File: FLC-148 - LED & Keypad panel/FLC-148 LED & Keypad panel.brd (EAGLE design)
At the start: 52 x 73.8 mm, 76 parts, among them IC1 MAX6818, IC2 MAX6818, IC3 NTGD3148NT1G, IC4 NTGD3148NT1G, IC5 STM32G071CBU6, IC6 ECS-480-10-33B-CKM-TR, J1 FTSH-107-01-L-DV-K-A

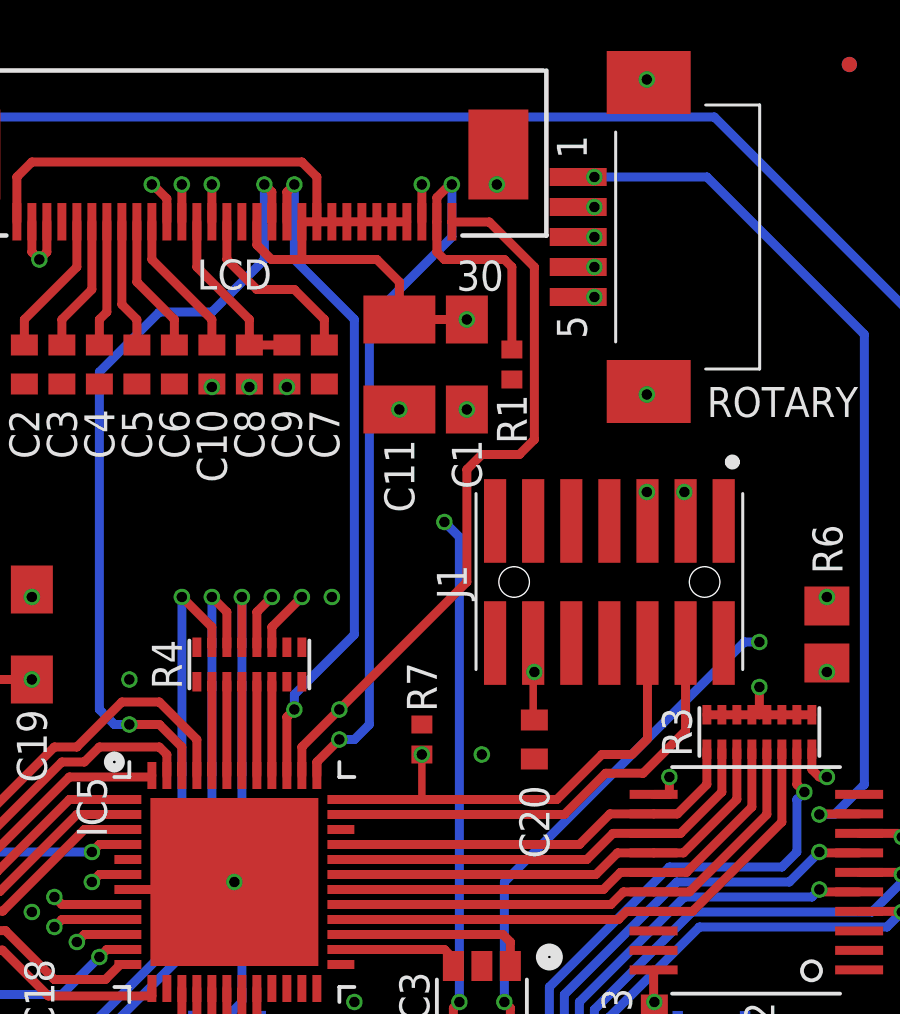
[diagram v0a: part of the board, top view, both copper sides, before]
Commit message: - routed missing LCD D/C pin to PA12
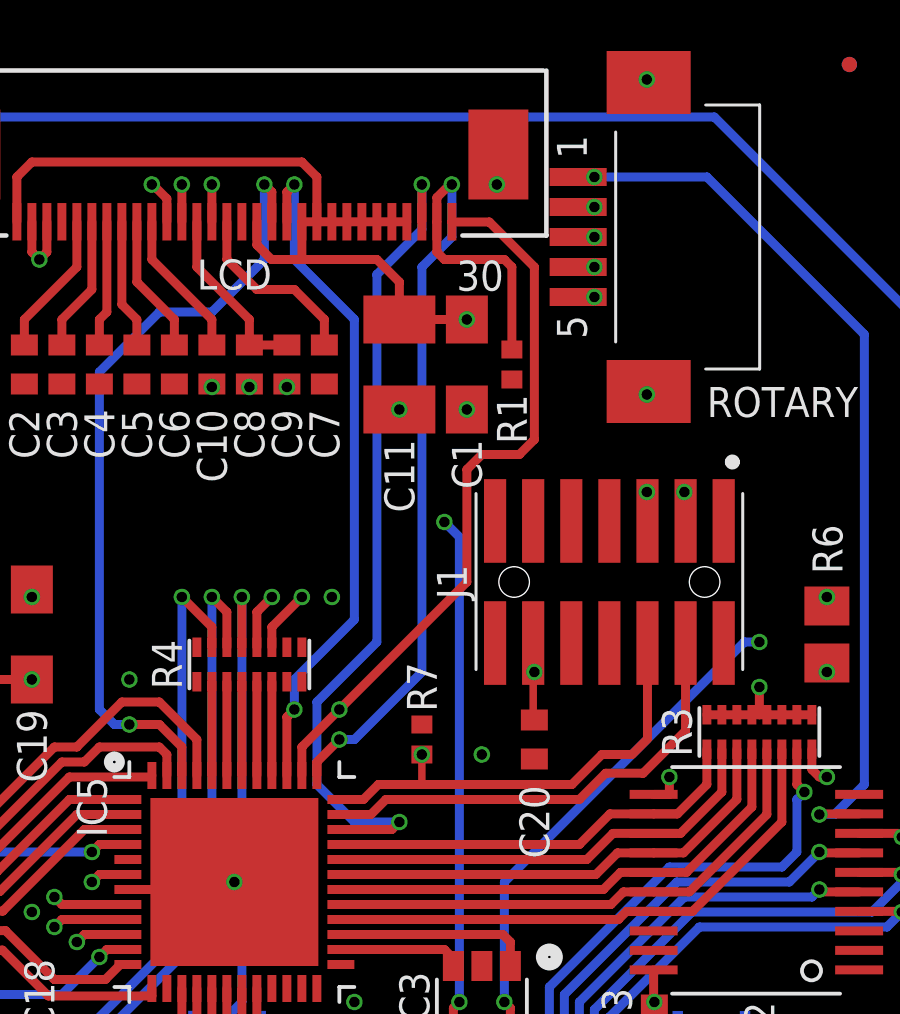
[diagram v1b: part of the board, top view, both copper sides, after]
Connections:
- net OLED_!D!/C: now also IC5.34_PA12[PA10]
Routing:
- net OLED_!D!/C: track 1.24 -> 28.0 mm, vias 1 -> 2
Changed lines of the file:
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@@
 <grid distance="0.25" unitdist="mm" unit="mm" style="dots" multiple="1" display="yes" altdistance="0.05" altunitdist="mm" altunit="mm"/>
 <layers>
-<layer number="1" name="Top" color="4" fill="1" visible="no" active="yes"/>
+<layer number="1" name="Top" color="4" fill="1" visible="yes" active="yes"/>
 <layer number="2" name="Route2" color="16" fill="1" visible="no" active="yes"/>
 <layer number="3" name="Route3" color="17" fill="1" visible="no" active="no"/>
@@
 <layer number="14" name="Route14" color="22" fill="1" visible="no" active="no"/>
 <layer number="15" name="Route15" color="23" fill="1" visible="no" active="yes"/>
-<layer number="16" name="Bottom" color="1" fill="1" visible="yes" active="yes"/>
+<layer number="16" name="Bottom" color="1" fill="1" visible="no" active="yes"/>
 <layer number="17" name="Pads" color="2" fill="1" visible="yes" active="yes"/>
 <layer number="18" name="Vias" color="2" fill="1" visible="yes" active="yes"/>
 <layer number="19" name="Unrouted" color="6" fill="1" visible="yes" active="yes"/>
 <layer number="20" name="Dimension" color="24" fill="1" visible="yes" active="yes"/>
-<layer number="21" name="tPlace" color="7" fill="1" visible="no" active="yes"/>
-<layer number="22" name="bPlace" color="7" fill="1" visible="yes" active="yes"/>
-<layer number="23" name="tOrigins" color="15" fill="1" visible="no" active="yes"/>
-<layer number="24" name="bOrigins" color="15" fill="1" visible="yes" active="yes"/>
-<layer number="25" name="tNames" color="7" fill="1" visible="no" active="yes"/>
-<layer number="26" name="bNames" color="7" fill="1" visible="yes" active="yes"/>
+<layer number="21" name="tPlace" color="7" fill="1" visible="yes" active="yes"/>
+<layer number="22" name="bPlace" color="7" fill="1" visible="no" active="yes"/>
+<layer number="23" name="tOrigins" color="15" fill="1" visible="yes" active="yes"/>
+<layer number="24" name="bOrigins" color="15" fill="1" visible="no" active="yes"/>
+<layer number="25" name="tNames" color="7" fill="1" visible="yes" active="yes"/>
+<layer number="26" name="bNames" color="7" fill="1" visible="no" active="yes"/>
 <layer number="27" name="tValues" color="7" fill="1" visible="no" active="yes"/>
 <layer number="28" name="bValues" color="7" fill="1" visible="no" active="yes"/>
-<layer number="29" name="tStop" color="7" fill="3" visible="no" active="yes"/>
-<layer number="30" name="bStop" color="7" fill="6" visible="yes" active="yes"/>
+<layer number="29" name="tStop" color="7" fill="3" visible="yes" active="yes"/>
+<layer number="30" name="bStop" color="7" fill="6" visible="no" active="yes"/>
 <layer number="31" name="tCream" color="7" fill="4" visible="no" active="yes"/>
 <layer number="32" name="bCream" color="7" fill="5" visible="no" active="yes"/>
@@
 <layer number="37" name="tTest" color="7" fill="1" visible="no" active="yes"/>
 <layer number="38" name="bTest" color="7" fill="1" visible="no" active="yes"/>
-<layer number="39" name="tKeepout" color="4" fill="11" visible="no" active="yes"/>
-<layer number="40" name="bKeepout" color="1" fill="11" visible="yes" active="yes"/>
-<layer number="41" name="tRestrict" color="4" fill="10" visible="no" active="yes"/>
-<layer number="42" name="bRestrict" color="1" fill="10" visible="yes" active="yes"/>
+<layer number="39" name="tKeepout" color="4" fill="11" visible="yes" active="yes"/>
+<layer number="40" name="bKeepout" color="1" fill="11" visible="no" active="yes"/>
+<layer number="41" name="tRestrict" color="4" fill="10" visible="yes" active="yes"/>
+<layer number="42" name="bRestrict" color="1" fill="10" visible="no" active="yes"/>
 <layer number="43" name="vRestrict" color="2" fill="10" visible="yes" active="yes"/>
 <layer number="44" name="Drills" color="7" fill="1" visible="no" active="yes"/>
@@
 <layer number="49" name="Reference" color="7" fill="1" visible="no" active="yes"/>
 <layer number="50" name="dxf" color="7" fill="1" visible="no" active="no"/>
-<layer number="51" name="tDocu" color="7" fill="1" visible="no" active="yes"/>
-<layer number="52" name="bDocu" color="7" fill="1" visible="yes" active="yes"/>
+<layer number="51" name="tDocu" color="7" fill="1" visible="yes" active="yes"/>
+<layer number="52" name="bDocu" color="7" fill="1" visible="no" active="yes"/>
 <layer number="53" name="tGND_GNDA" color="7" fill="1" visible="no" active="no"/>
 <layer number="54" name="bGND_GNDA" color="7" fill="1" visible="no" active="no"/>
@@
 <contactref element="J1" pad="4"/>
 <contactref element="IC5" pad="35_PA13"/>
-<wire x1="29.8" y1="35" x2="37.25" y2="35" width="0.3" layer="1"/>
-<wire x1="37.25" y1="35" x2="38.625" y2="36.375" width="0.3" layer="1"/>
+<wire x1="37.75" y1="35.5" x2="31.3" y2="35.5" width="0.3" layer="1"/>
+<wire x1="31.3" y1="35.5" x2="30.8" y2="35" width="0.3" layer="1"/>
+<wire x1="29.8" y1="35" x2="30.8" y2="35" width="0.3" layer="1"/>
+<wire x1="37.75" y1="35.5" x2="38.625" y2="36.375" width="0.3" layer="1"/>
 <wire x1="38.625" y1="36.375" x2="39.875" y2="36.375" width="0.3" layer="1"/>
 <wire x1="39.875" y1="36.375" x2="41.29" y2="37.79" width="0.3" layer="1"/>
@@
 <wire x1="29" y1="36.3" x2="29" y2="36.75" width="0.3" layer="1"/>
 <wire x1="29.75" y1="37.5" x2="29" y2="36.75" width="0.3" layer="1"/>
-<wire x1="30.25" y1="37.5" x2="30.75" y2="38" width="0.3" layer="16"/>
+<wire x1="30.25" y1="37.5" x2="32.5" y2="39.75" width="0.3" layer="16"/>
 <wire x1="29.75" y1="37.5" x2="30.25" y2="37.5" width="0.3" layer="16"/>
-<wire x1="30.75" y1="38" x2="30.75" y2="51.5" width="0.3" layer="16"/>
-<wire x1="30.75" y1="51.5" x2="33.5" y2="54.25" width="0.3" layer="16"/>
+<wire x1="32.5" y1="39.75" x2="32.5" y2="53.25" width="0.3" layer="16"/>
+<wire x1="32.5" y1="53.25" x2="33.5" y2="54.25" width="0.3" layer="16"/>
 <wire x1="35.5" y1="50.5" x2="35.5" y2="53.25" width="0.3" layer="1"/>
 <wire x1="35.25" y1="53.5" x2="33.25" y2="53.5" width="0.3" layer="1"/>
@@
 <via x="32.5" y="56" extent="1-16" drill="0.35"/>
 <wire x1="32.5" y1="54.757" x2="32.5" y2="56" width="0.3" layer="1"/>
+<contactref element="IC5" pad="34_PA12[PA10]"/>
+<via x="31.75" y="34.75" extent="1-16" drill="0.35"/>
+<wire x1="29.8" y1="34.5" x2="31.5" y2="34.5" width="0.3" layer="1"/>
+<wire x1="31.5" y1="34.5" x2="31.75" y2="34.75" width="0.3" layer="1"/>
+<wire x1="31.75" y1="34.75" x2="30.25" y2="34.75" width="0.3" layer="16"/>
+<wire x1="30.25" y1="34.75" x2="29" y2="36" width="0.3" layer="16"/>
+<wire x1="29" y1="38.75" x2="31" y2="40.75" width="0.3" layer="16"/>
+<wire x1="29" y1="36" x2="29" y2="38.75" width="0.3" layer="16"/>
+<wire x1="32.5" y1="54.5" x2="32.5" y2="56" width="0.3" layer="16"/>
+<wire x1="31" y1="40.75" x2="31" y2="53" width="0.3" layer="16"/>
+<wire x1="31" y1="53" x2="32.5" y2="54.5" width="0.3" layer="16"/>
 </signal>
 <signal name="MCU_KEYPAD_INTERRUPT" class="2">
@@
 <contactref element="J1" pad="6"/>
 <contactref element="IC5" pad="36_PA14-BOOT0"/>
-<wire x1="37" y1="35.5" x2="32.5" y2="35.5" width="0.3" layer="1"/>
-<wire x1="32.5" y1="35.5" x2="29.8" y2="35.5" width="0.3" layer="1"/>
-<wire x1="37" y1="35.5" x2="38.5" y2="37" width="0.3" layer="1"/>
+<wire x1="37.5" y1="36" x2="32.25" y2="36" width="0.3" layer="1"/>
+<wire x1="32.5" y1="36" x2="31.05" y2="36" width="0.3" layer="1"/>
+<wire x1="31.05" y1="36" x2="30.55" y2="35.5" width="0.3" layer="1"/>
+<wire x1="30.55" y1="35.5" x2="29.8" y2="35.5" width="0.3" layer="1"/>
+<wire x1="37.5" y1="36" x2="38.5" y2="37" width="0.3" layer="1"/>
 <wire x1="38.5" y1="37" x2="39.5" y2="37" width="0.3" layer="1"/>
 <wire x1="39.5" y1="37" x2="40.02" y2="37.52" width="0.3" layer="1"/>
 <wire x1="40.02" y1="37.52" x2="40.02" y2="40.715" width="0.3" layer="1"/>
 <contactref element="R7" pad="2"/>
-<wire x1="32.5" y1="37" x2="32.5" y2="35.5" width="0.25" layer="1"/>
+<wire x1="32.5" y1="37" x2="32.5" y2="36" width="0.25" layer="1"/>
 <contactref element="MCU" pad="12_PD14"/>
 <via x="24.5" y="20.75" extent="1-16" drill="0.35"/>
@@
 <wire x1="28.25" y1="38.5" x2="28" y2="38.25" width="0.3" layer="1"/>
 <wire x1="28" y1="36.3" x2="28" y2="38.25" width="0.3" layer="1"/>
-<wire x1="28.25" y1="38.5" x2="28.25" y2="39" width="0.3" layer="16"/>
-<wire x1="30.25" y1="41" x2="28.25" y2="39" width="0.3" layer="16"/>
-<wire x1="30.25" y1="41" x2="30.25" y2="51.5" width="0.3" layer="16"/>
+<wire x1="28.25" y1="38.5" x2="28.25" y2="39.5" width="0.3" layer="16"/>
+<wire x1="30.25" y1="41.5" x2="28.25" y2="39.5" width="0.3" layer="16"/>
+<wire x1="30.25" y1="41.5" x2="30.25" y2="51.5" width="0.3" layer="16"/>
 <wire x1="30.25" y1="51.5" x2="28.25" y2="53.5" width="0.3" layer="16"/>
 <wire x1="28.25" y1="53.5" x2="28.25" y2="56" width="0.3" layer="16"/>
@@
 <wire x1="40.225" y1="35.67" x2="40.75" y2="35.67" width="0.3" layer="1"/>
 <wire x1="40.75" y1="35.67" x2="40.75" y2="36.25" width="0.3" layer="1"/>
-<wire x1="30.5" y1="35.25" x2="25.5" y2="30.25" width="0.4" layer="2"/>
+<wire x1="30.75" y1="35.5" x2="25.5" y2="30.25" width="0.4" layer="2"/>
 <wire x1="21.75" y1="30.25" x2="25.5" y2="30.25" width="0.4" layer="2"/>
-<wire x1="39.75" y1="35.25" x2="40.75" y2="36.25" width="0.4" layer="2"/>
-<wire x1="39.75" y1="35.25" x2="30.5" y2="35.25" width="0.4" layer="2"/>
+<wire x1="40" y1="35.5" x2="40.75" y2="36.25" width="0.4" layer="2"/>
+<wire x1="40" y1="35.5" x2="30.75" y2="35.5" width="0.4" layer="2"/>
 </signal>
 <signal name="VBAT">

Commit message: - renamed signals to be more consistent
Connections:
- net BACKLIGHT_GREEN_DRAIN renamed LCD_BACKLIGHT_GREEN_DRAIN
- net BACKLIGHT_IR_DRAIN renamed LCD_BACKLIGHT_IR_DRAIN
- net KEYPAD_IR_LED_DRAIN renamed KEYPAD_BACKLIGHT_IR_DRAIN
- net LED_BACKLIGHT_GREEN_GATE renamed OLED_BACKLIGHT_GREEN_GATE
- net LED_BACKLIGHT_IR_GATE renamed OLED_BACKLIGHT_IR_GATE
- net SPI_LCD_MOSI renamed SPI_OLED_MOSI
- net SPI_LCD_SCK renamed SPI_OLED_SCK
- net SPI_LCD_SS renamed SPI_OLED_SS
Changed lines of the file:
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@@
 <wire x1="26.75" y1="22.4925125" x2="26.75" y2="18.96" width="0.3" layer="1"/>
 </signal>
-<signal name="SPI_LCD_SCK" class="2">
+<signal name="SPI_OLED_SCK" class="2">
 <contactref element="LCD" pad="19_DB6"/>
 <via x="28.25" y="56" extent="1-16" drill="0.35"/>
@@
 <wire x1="28.25" y1="53.5" x2="28.25" y2="56" width="0.3" layer="16"/>
 </signal>
-<signal name="SPI_LCD_MOSI" class="2">
+<signal name="SPI_OLED_MOSI" class="2">
 <contactref element="LCD" pad="18_DB7"/>
 <via x="27.25" y="56" extent="1-16" drill="0.35"/>
@@
 <wire x1="21.75" y1="49.75" x2="21.75" y2="38.5" width="0.3" layer="16"/>
 </signal>
-<signal name="SPI_LCD_SS" class="2">
+<signal name="SPI_OLED_SS" class="2">
 <contactref element="LCD" pad="30_!CS1!"/>
 <contactref element="IC5" pad="38_PD0"/>
@@
 <wire x1="34" y1="42.75" x2="34" y2="46.5" width="0.3" layer="1"/>
 </signal>
-<signal name="LED_BACKLIGHT_GREEN_GATE" class="2">
+<signal name="OLED_BACKLIGHT_GREEN_GATE" class="2">
 <contactref element="IC5" pad="27_PB15"/>
 <contactref element="IC3" pad="1_G1"/>
@@
 <wire x1="29.8" y1="31" x2="35.2" y2="31" width="0.3" layer="1"/>
 </signal>
-<signal name="LED_BACKLIGHT_IR_GATE" class="2">
+<signal name="OLED_BACKLIGHT_IR_GATE" class="2">
 <contactref element="IC5" pad="26_PB14"/>
 <contactref element="IC3" pad="3_G2"/>
@@
 <wire x1="46" y1="41.95" x2="46" y2="42.25" width="0.3" layer="1"/>
 </signal>
-<signal name="BACKLIGHT_GREEN_DRAIN" class="2">
+<signal name="LCD_BACKLIGHT_GREEN_DRAIN" class="2">
 <contactref element="IC3" pad="6_D1"/>
 <via x="35.25" y="28.75" extent="1-16" drill="0.35"/>
@@
 <wire x1="50.45" y1="40.75" x2="50.5" y2="40.8" width="0.3" layer="16"/>
 </signal>
-<signal name="BACKLIGHT_IR_DRAIN" class="2">
+<signal name="LCD_BACKLIGHT_IR_DRAIN" class="2">
 <contactref element="IC3" pad="4_D2"/>
 <via x="33.75" y="28.75" extent="1-16" drill="0.35"/>
@@
 <wire x1="48.25" y1="44.25" x2="48.25" y2="44.75" width="0.4" layer="2"/>
 </signal>
-<signal name="KEYPAD_IR_LED_DRAIN" class="2">
+<signal name="KEYPAD_BACKLIGHT_IR_DRAIN" class="2">
 <contactref element="LED5" pad="C"/>
 <contactref element="LED8" pad="C"/>

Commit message: - replaced 1mm 5p zif connector (52793-0570) with better part (52207-0533)
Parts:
- PTT, ROTARY: value 52793-0570 -> 52207-0533
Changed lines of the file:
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@@
 <attribute name="VALUE" x="43.75" y="35.75" size="1" layer="27" font="vector" align="center"/>
 </element>
-<element name="PTT" library="527930570 FFC Connector 5p 1mm Pitch" package="SMD" value="52793-0570" x="37.75" y="15" smashed="yes" rot="R90">
+<element name="PTT" library="527930570 FFC Connector 5p 1mm Pitch" package="SMD" value="52207-0533" x="37.75" y="15" smashed="yes" rot="R90">
 <attribute name="NAME" x="38.25" y="9.5" size="1" layer="25" font="vector" rot="R180" align="center-right"/>
 <attribute name="VALUE" x="41.75" y="15" size="1" layer="27" font="vector" rot="R90" align="center"/>
@@
 <attribute name="VALUE" x="19.155" y="40.365" size="1.27" layer="27" rot="R90"/>
 </element>
-<element name="ROTARY" library="527930570 FFC Connector 5p 1mm Pitch" package="SMD" value="52793-0570" x="41.5" y="54.25" smashed="yes" rot="R90">
+<element name="ROTARY" library="527930570 FFC Connector 5p 1mm Pitch" package="SMD" value="52207-0533" x="41.5" y="54.25" smashed="yes" rot="R90">
 <attribute name="NAME" x="42" y="48.75" size="1" layer="25" font="vector" align="center-left"/>
 <attribute name="VALUE" x="45.5" y="54.25" size="1" layer="27" font="vector" rot="R90" align="center"/>

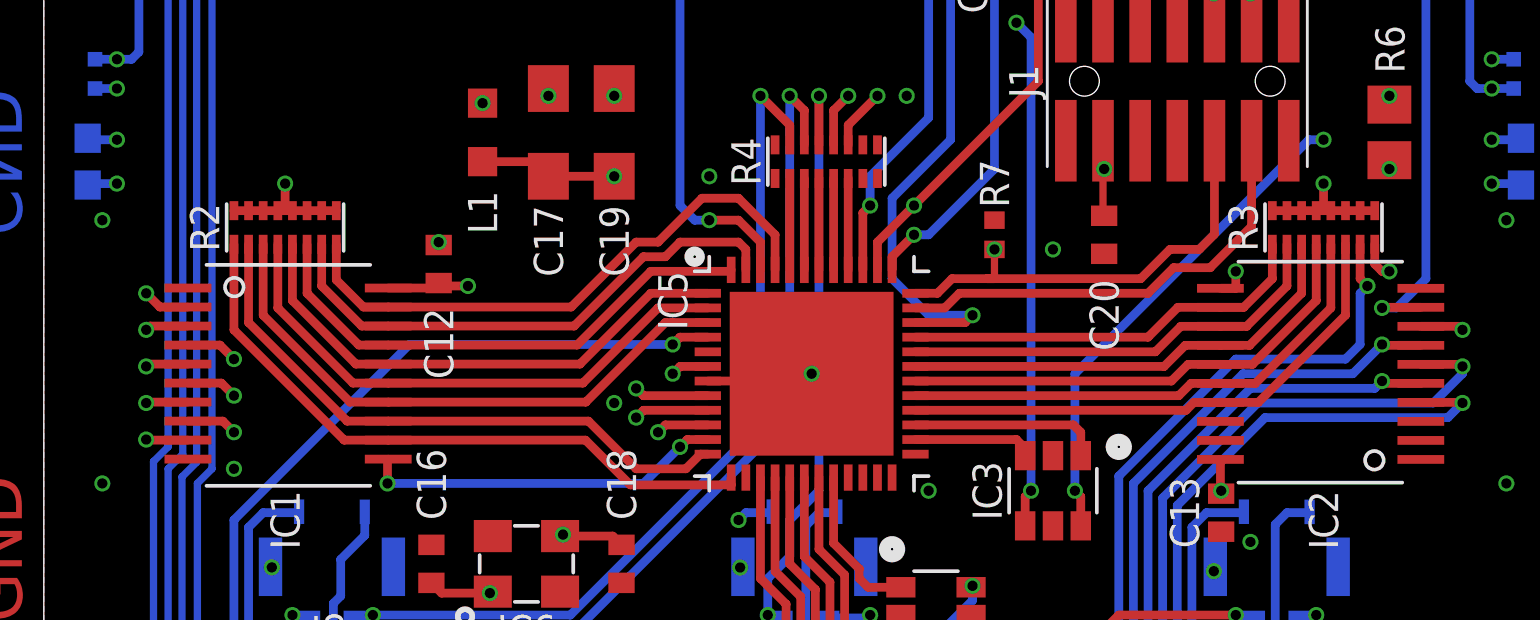
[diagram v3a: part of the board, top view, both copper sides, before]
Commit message: - started to remove 10k resistor arrays since pullups in the stm32 can replace them
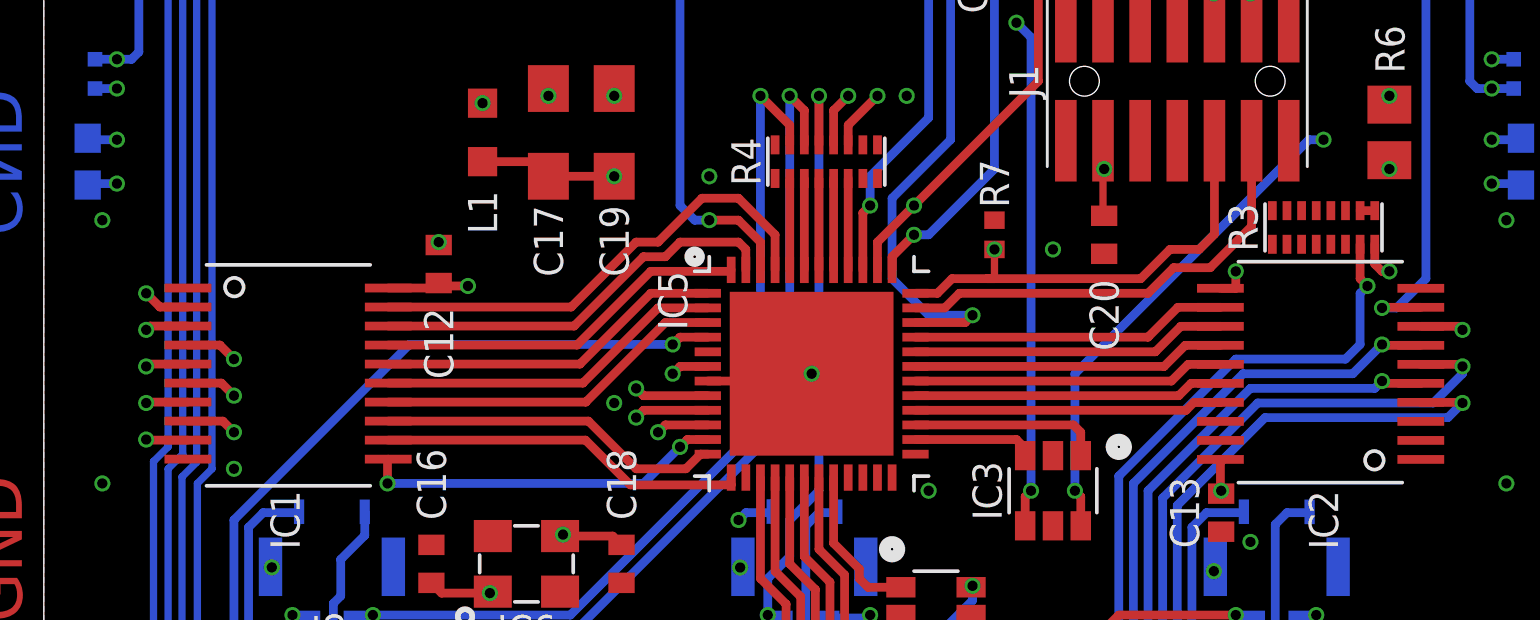
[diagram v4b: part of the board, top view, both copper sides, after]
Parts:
- removed R2: 741X163103JP - 10K, 741X163103JP 10k Ohm Resistor Array:SMD
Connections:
- net 3V3: no longer R2.P$10, R2.P$11, R2.P$12, R2.P$13, R2.P$14, R2.P$15, R2.P$16, R2.P$9, R3.P$11, R3.P$12, R3.P$13, R3.P$14, R3.P$15, R3.P$16
- net ALT_OUT: no longer R2.P$5
- net DOWN_OUT: no longer R2.P$2
- net ENT_OUT: no longer R2.P$1
- net ESC_OUT: no longer R2.P$7
- net FN1_OUT: no longer R3.P$4
- net FN2_OUT: no longer R3.P$6
- net GR_OUT: no longer R2.P$4
- net MODE_OUT: no longer R2.P$6
- net PTT_OUT: no longer R3.P$3
- net ROTARY_A_OUT: no longer R3.P$2
- net ROTARY_B_OUT: no longer R2.P$8
- net ROTARY_PUSH_OUT: no longer R3.P$1
- net SQL_OUT: no longer R3.P$5
- net UP_OUT: no longer R2.P$3
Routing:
- net ENT_OUT: track 22.4 -> 12.6 mm
- net DOWN_OUT: track 20.7 -> 11.8 mm
- net 3V3: track 48.9 -> 40.5 mm, vias 15 -> 13
- net FN2_OUT: track 18.7 -> 10.8 mm
- net UP_OUT: track 20.0 -> 12.1 mm
- net SQL_OUT: track 17.6 -> 10.6 mm
- net GR_OUT: track 19.0 -> 12.0 mm
- net FN1_OUT: track 16.8 -> 10.7 mm
- net ALT_OUT: track 18.0 -> 11.9 mm
- net PTT_OUT: track 15.9 -> 10.7 mm
- net MODE_OUT: track 18.0 -> 12.8 mm
- net ROTARY_A_OUT: track 15.1 -> 10.8 mm
- net ESC_OUT: track 18.5 -> 14.2 mm
- net ROTARY_B_OUT: track 19.9 -> 16.5 mm
- net ROTARY_PUSH_OUT: track 14.2 -> 10.8 mm
